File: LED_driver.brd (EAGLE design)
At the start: 38.6 x 25.4 mm, 16 parts

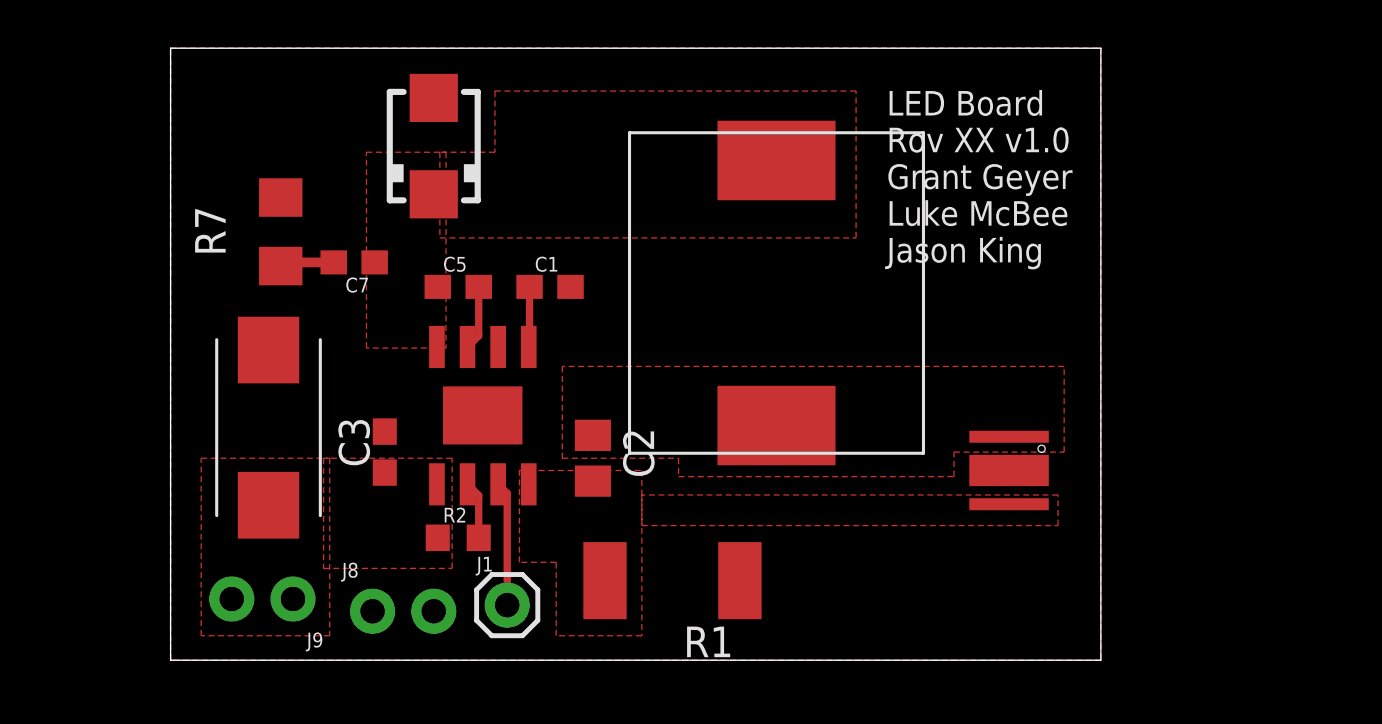
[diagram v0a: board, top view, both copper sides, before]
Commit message: Finishing up routing
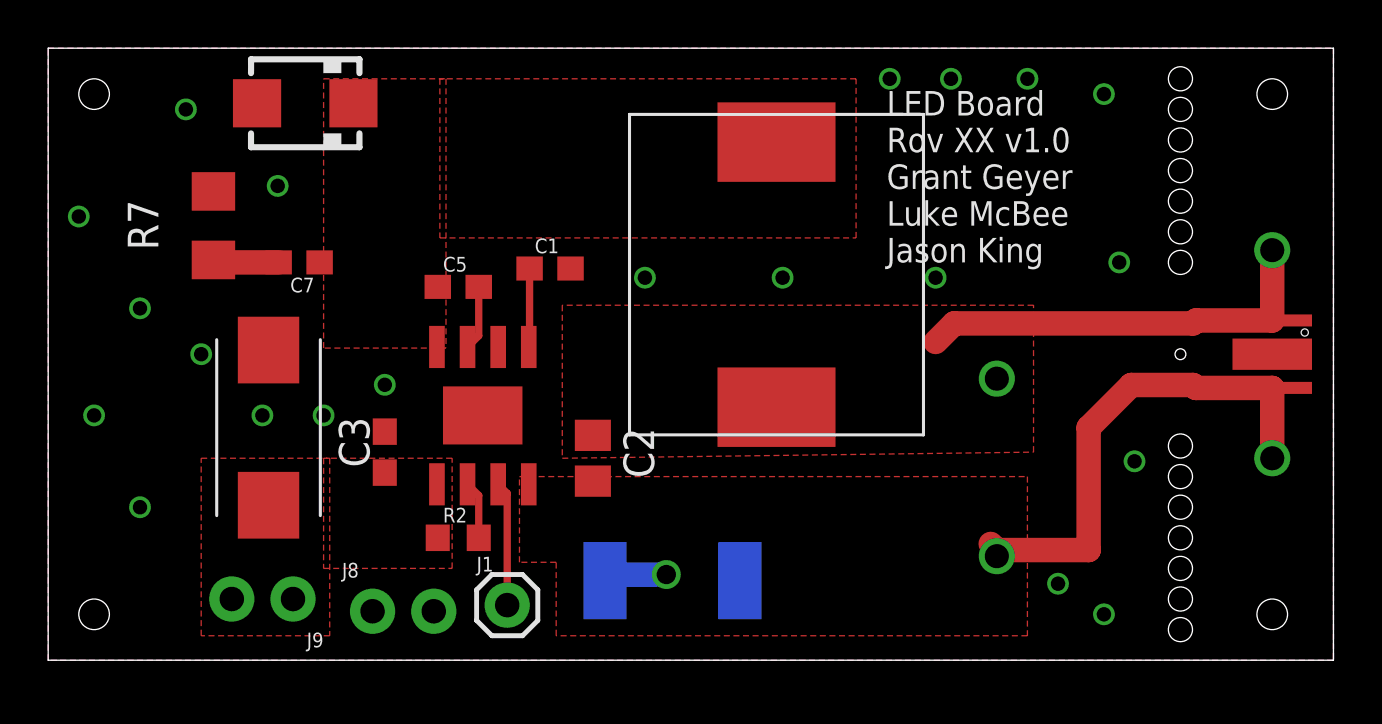
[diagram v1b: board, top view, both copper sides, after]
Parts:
- moved U$3 11.9 mm to (45.7, 12.7)
- moved D1 5.62 mm to (5.59, 23.1), turned to 180 degrees
- moved R7 2.81 mm to (1.78, 18.0)
- moved C7 2.29 mm to (5.33, 16.5)
- moved C1 0.76 mm to (15.7, 16.3)
- moved U$4 0.76 mm to (25.1, 16.0)
- flipped R1 to the bottom, turned to 0 degrees
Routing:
- net LED-: track 0.00 -> 23.2 mm, vias 0 -> 3
- net LED+: track 0.00 -> 17.3 mm, vias 0 -> 2
- net VCC6211: track 2.58 -> 3.34 mm
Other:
- board size 38.6 x 25.4 mm -> 53.3 x 25.4 mm
